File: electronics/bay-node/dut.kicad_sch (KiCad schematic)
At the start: 26 parts, among them J5 AUX, J6 CAM, Q2 2N7002, Q3 2N7002, U10 INA226AIDGSR, U9 TPS2553DBVR

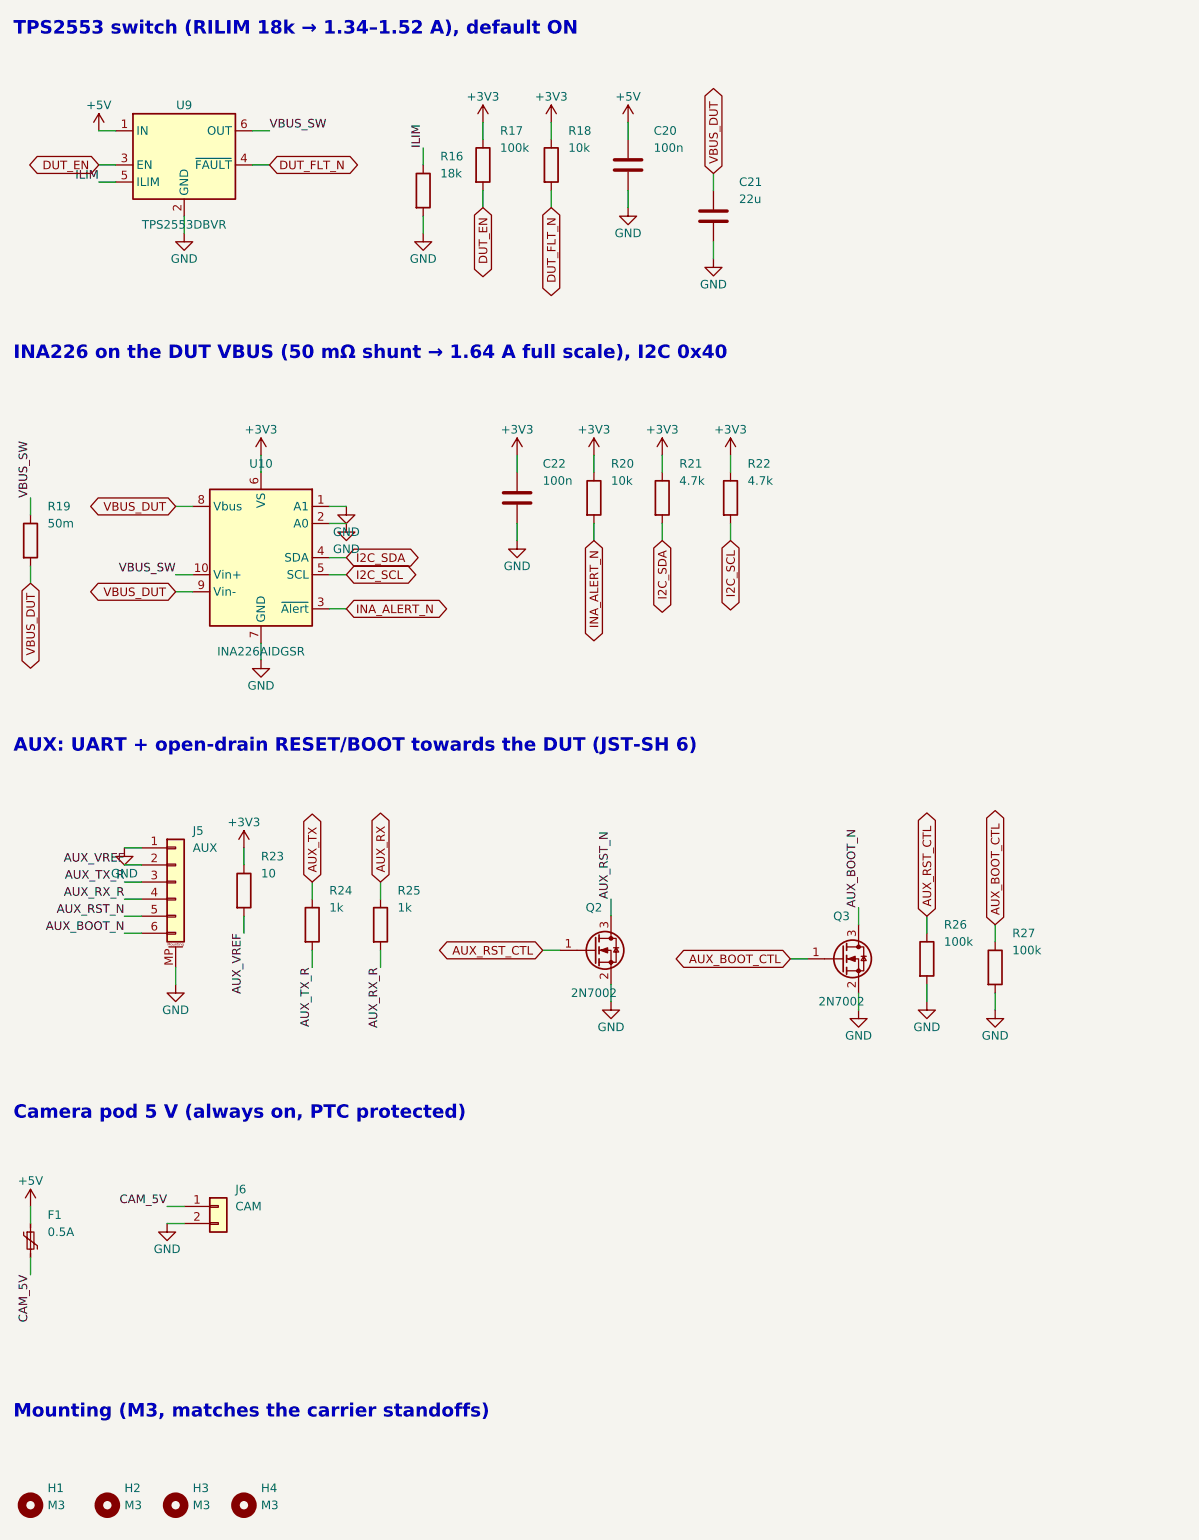
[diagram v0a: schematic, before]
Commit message: Schematics: draw real wires and an overview block diagram
The generator used to connect every pin through a net label only. Now,
in each block, the part with the most pins is the anchor and the
two-pin parts that share a signal with one of its side pins hang off
that pin on a real wire; parts chained behind them (R -> C -> GND)
stack underneath, and anchor-less blocks (pull-ups, reset/boot
buttons) are adopted by the anchor they connect to. Power symbols on
side pins point outward; power-flag references are hidden.

The root sheet becomes a block diagram: the supply rails each sheet
uses across the top, and one lane per pair of sheets listing the
signals they share.

Every wired net still carries one label, so net names, ERC (0) and the
PCB's schematic parity (0) are unchanged; the routed PCBs are untouched.

Co-Authored-By: Claude Opus 5.5 <noreply@anthropic.com>
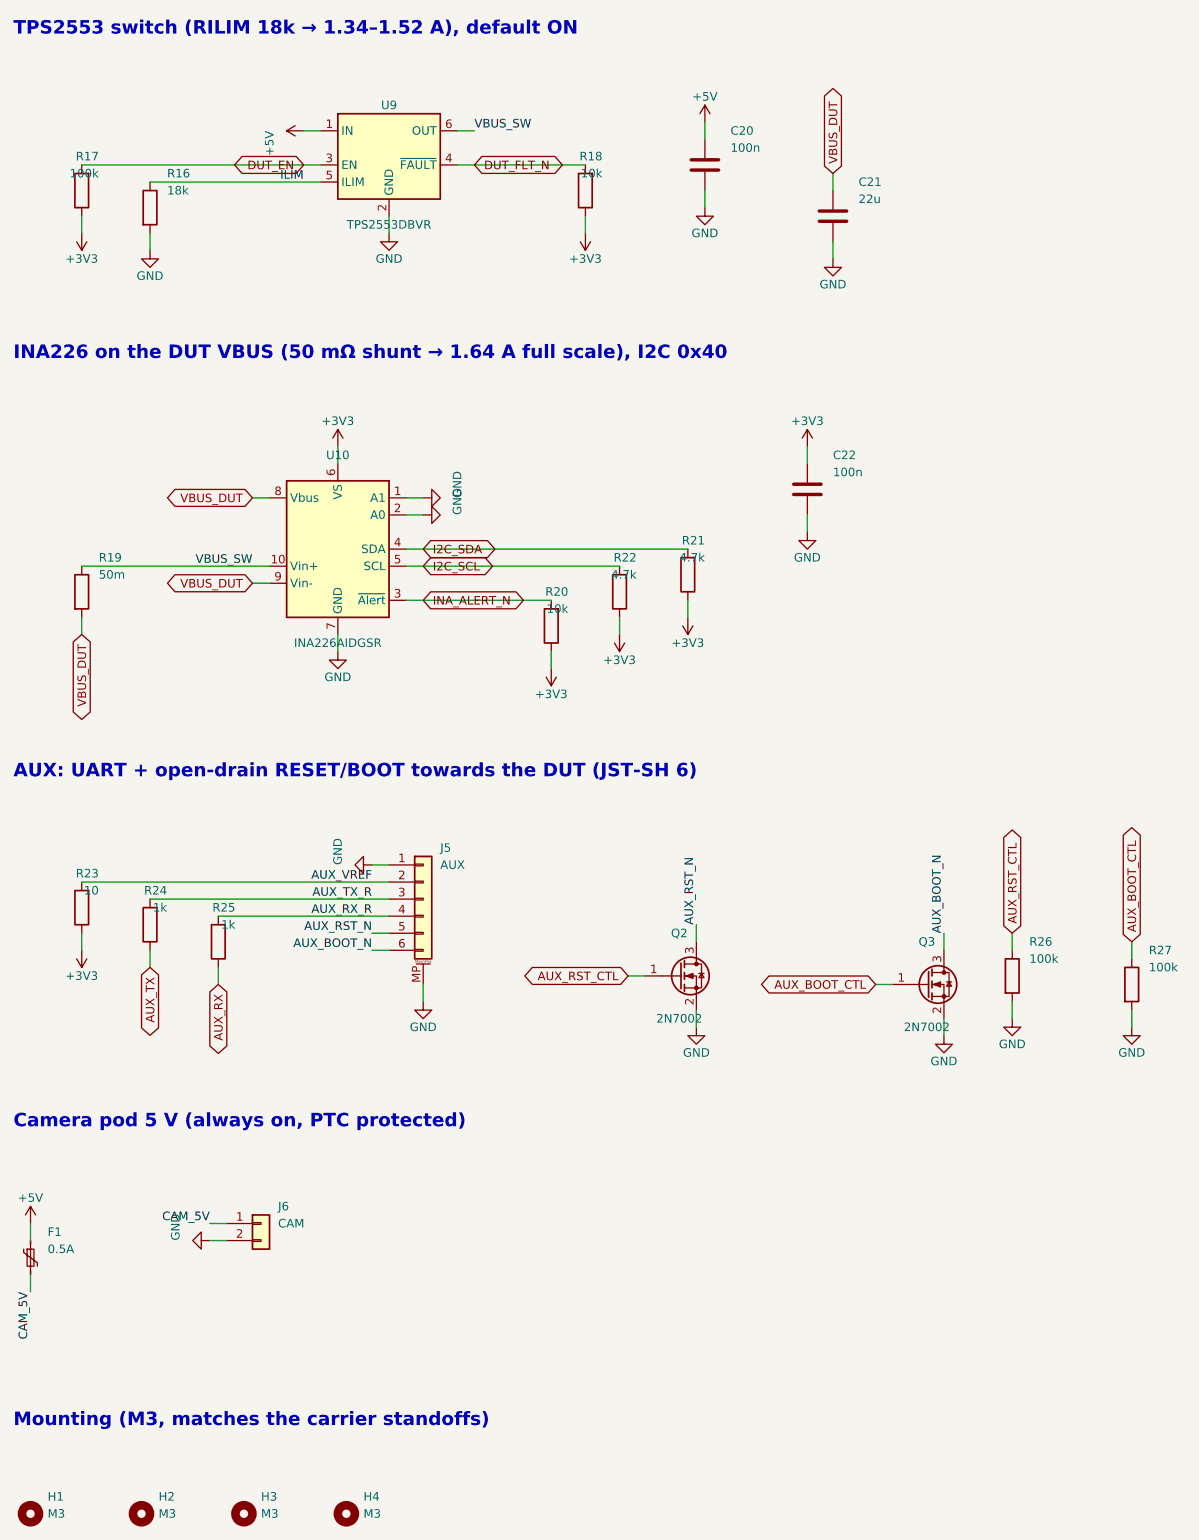
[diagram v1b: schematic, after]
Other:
- moved on the sheet: C20, C21, C22, F1, H1, H2, H3, H4, J5, J6, Q2, Q3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

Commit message: Boards v0.2: LMR51635 buck, JST PH, drawn schematics, thermal reliefs
Addresses Fabio's review of v0.1.

Bay node (rev 0.2):
- 5 V buck: LMR51635YDDCR (60 V, 3.5 A, synchronous, 1.1 MHz) with a
  3.3 uH FXL0630, 3 x 22 uF out, 2 x 10 uF + 100 nF in, FB 120k/22k
  (5.16 V), EN 1M/100k UVLO (13.5 V on, 10.8 V off). Replaces the
  TPS54360B, its Schottky and compensation network. CIN straddles the
  VIN/GND pins on solid top-side islands with vias to In1 (TI SLUSF64B).
- 24 V in/out on JST PH (carrier notches resized, rack.yaml pwr_y).
- Power nets named along the path: 24V_BUS -> +24V -> +5V -> DUT_5V_SW
  -> shunt -> DUT_5V; the INA226 visibly runs from +3V3.
- Stackup S+GND / GND / PWR / S+GND: In2 carries +5V, +3V3 under the
  ESP32 and a protected 24 V bus strip. Outer GND pours kept (without
  them Freerouting left ~25 connections unrouted).

Power hub (rev 0.2): JST VH input instead of the screw terminal, JST PH
row outputs, eFuse limit 1.6 A (RILIM 7.5k) to protect the 2 A contacts.

Generator:
- eda.py: drawn schematic mode (sch= placement, Sheet.wire/tag/frame,
  rotated/mirrored symbols, automatic junctions, per-island labels and
  checks that no wire touches another net); all seven sheets redrawn.
- pcbgen.py: thermal reliefs on every pour (+ <board>.kicad_dru for
  single spokes on fine pitch), configurable inner layers, per-zone
  deferral, fixed vias, DRC-driven fix-up for isolated GND pads.
- JLC CPL fix for the LMR51635 (270 deg); BOM, cables, viewer, docs.

ERC 0, DRC 0 copper errors, 0 unconnected, schematic parity 0 on both.

Co-Authored-By: Claude Opus 5.5 <noreply@anthropic.com>
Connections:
- net ILIM renamed DUT_ILIM
- net VBUS_DUT renamed DUT_5V
- net VBUS_SW renamed DUT_5V_SW
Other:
- note added: "AUX: UART + open-drain RESET / BOOT towards the DUT (JST SH 6)"
- note added: "Camera pod 5 V (always on, PTC protected, JST PH)"
- note added: "DUT power path: +5V → TPS2553 switch → 50 mΩ shunt → DUT_5V (DUT port VBUS), INA226 across the shunt"
- note added: "I2C pull-ups"
- note removed: "AUX: UART + open-drain RESET/BOOT towards the DUT (JST-SH 6)"
- note removed: "Camera pod 5 V (always on, PTC protected)"
- note removed: "INA226 on the DUT VBUS (50 mΩ shunt → 1.64 A full scale), I2C 0x40"
- note removed: "TPS2553 switch (RILIM 18k → 1.34–1.52 A), default ON"
- moved on the sheet: C20, C21, C22, F1, H1, H2, H3, H4, J5, J6, Q2, Q3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

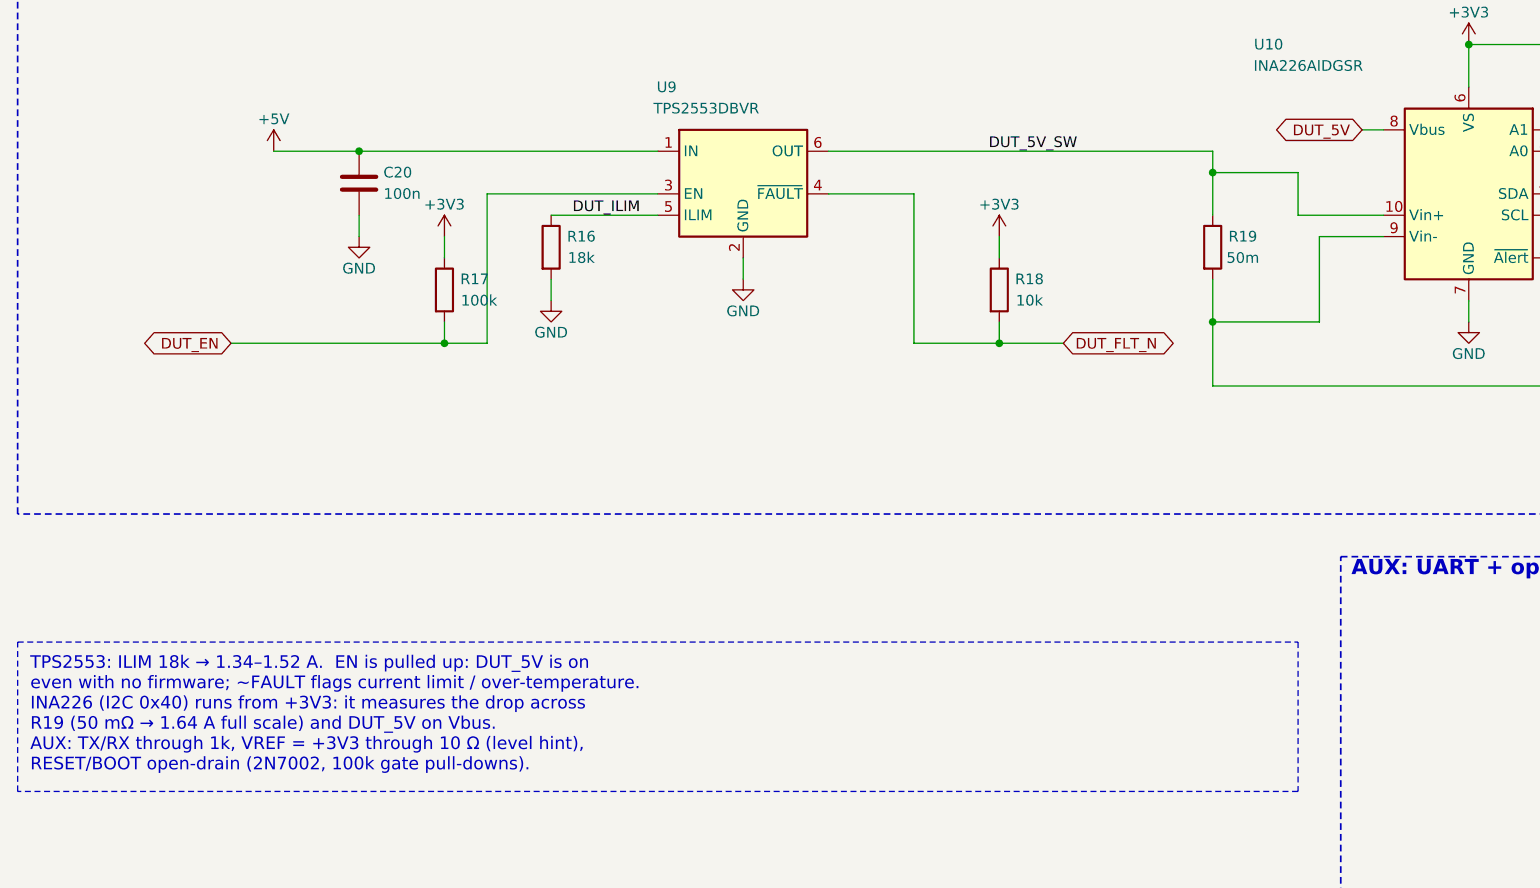
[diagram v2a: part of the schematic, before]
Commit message: Bay node: Kelvin shunt for the INA226, hand-routed USB High-Speed path
Kelvin shunt (review finding B4)
- R19 is Device:R_Shunt on bench:R_1206_3216Metric_Kelvin: the stock 1206
  pads plus a tented sense pad on the inner edge of each terminal, tied by
  net-tie pad groups (generated by the new electronics/tools/footprints.py).
- The INA226 reads SHUNT_P/SHUNT_N from those pads only, instead of tapping
  DUT_5V ~2.8 mm down the load track (~4-5 % gain error).

USB High-Speed in classic mode (finding B3)
- usb_hs_routes() in design.py draws the J3 -> U4 -> U5 -> U6 -> U8 -> J4
  chain as coupled pairs on F.Cu over In1 (0.25/0.15 mm, ~90 ohm estimate),
  ESD parts in flow-through, one B.Cu crossover between the FSUSB42s with
  three length bumps on PCPATH_DP; skew 1.8 mm J3 -> J4.  U4, U5, U6, U8,
  C17, C18, R24, R25 moved or rotated for a straight path.
- pcbgen.py: b.pcb["tracks"] draws locked tracks before routing (Freerouting
  keeps protected wiring and routes around it); fixed vias are locked too;
  pass-through vias left by Freerouting are dropped after the session import.

ERC 0/0, DRC 0 errors / 0 warnings, 0 unconnected, parity 0, JLC DFM audit
0 findings.  The power hub still regenerates clean with the new generator
(its committed outputs are unchanged).

Co-Authored-By: Claude Opus 5.5 <noreply@anthropic.com>
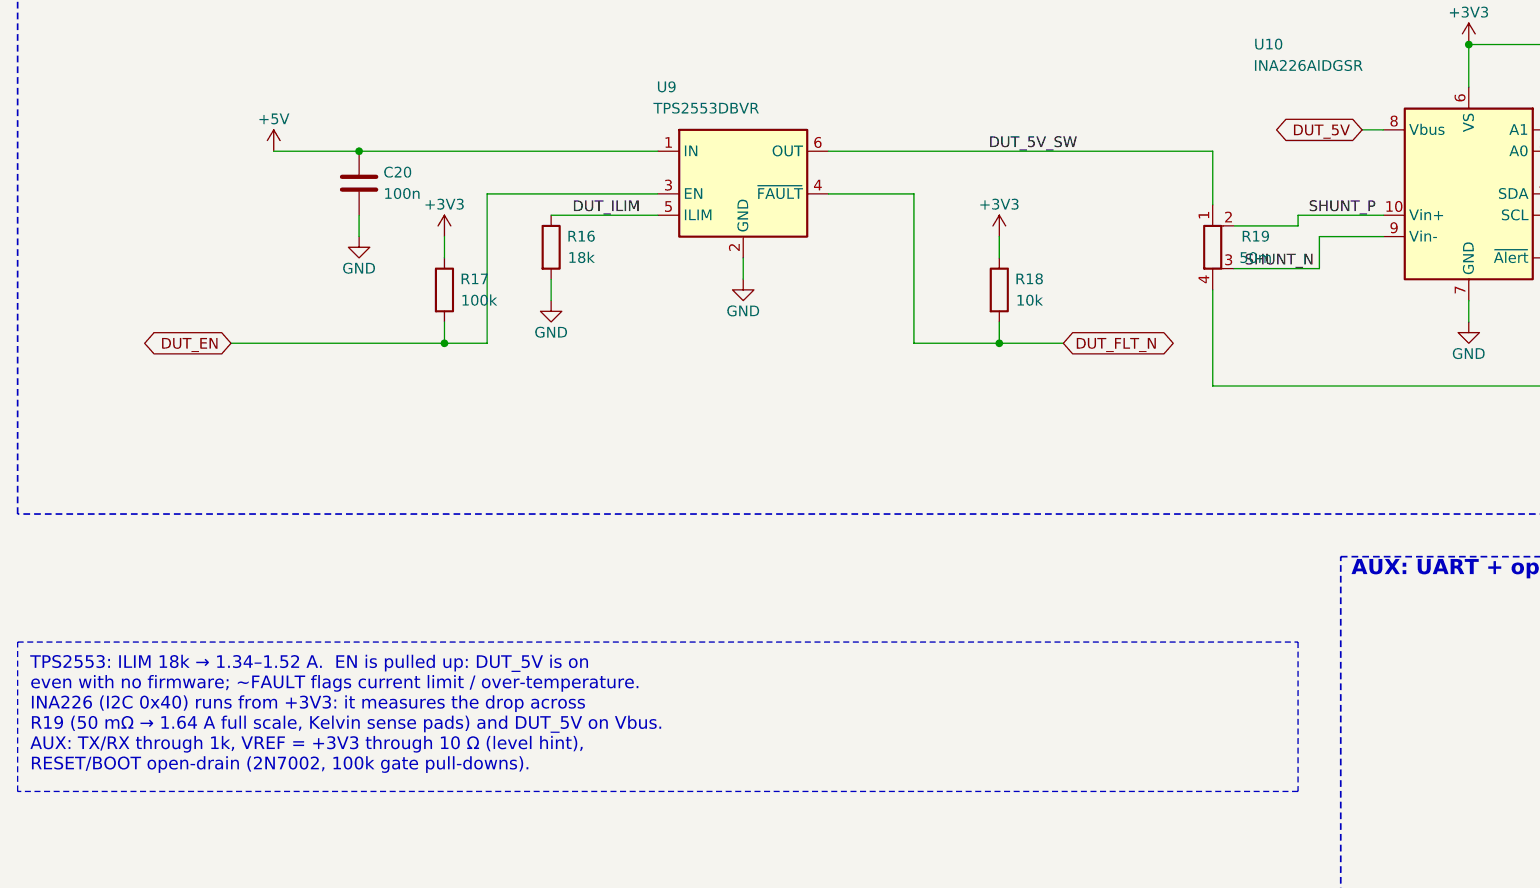
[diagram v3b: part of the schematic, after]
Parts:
- R19: footprint Resistor_SMD:R_1206_3216Metric -> bench:R_1206_3216Metric_Kelvin; symbol Device:R -> Device:R_Shunt
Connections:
- net DUT_5V: now also R19.4; no longer R19.2, U10.9 (Vin-)
- net DUT_5V_SW: no longer U10.10 (Vin+)
- new net SHUNT_N: R19.3, U10.9 (Vin-)
- new net SHUNT_P: R19.2, U10.10 (Vin+)
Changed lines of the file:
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@@
 	)
 	(symbol
-		(lib_id "Device:R")
+		(lib_id "Device:R_Shunt")
 		(at 157.48 85.09 0)
 		(unit 1)
@@
 		(fields_autoplaced yes)
 		(property "Reference" "R19"
-			(at 161.071 83.82 0)
+			(at 162.595 83.82 0)
 			(effects
 				(font
@@
 		)
 		(property "Value" "50m"
-			(at 161.071 86.36 0)
+			(at 162.595 86.36 0)
 			(effects
 				(font
@@
 			)
 		)
-		(property "Footprint" "Resistor_SMD:R_1206_3216Metric"
+		(property "Footprint" "bench:R_1206_3216Metric_Kelvin"
 			(at 157.48 85.09 0)
 			(effects
@@
 		(pin "2"
 		)
+		(pin "3"
+		)
+		(pin "4"
+		)
 		(instances
 			(project "bay-node"
@@
 		(pts
 			(xy 157.48 73.66)
-			(xy 157.48 81.28)
+			(xy 157.48 80.01)
 		)
 		(stroke
@@
 	(wire
 		(pts
-			(xy 157.48 88.9)
+			(xy 157.48 90.17)
 			(xy 157.48 101.6)
 		)
@@
 	(wire
 		(pts
-			(xy 157.48 76.2)
-			(xy 167.64 76.2)
+			(xy 160.02 82.55)
+			(xy 167.64 82.55)
 		)
 		(stroke
@@
 	(wire
 		(pts
-			(xy 167.64 76.2)
+			(xy 167.64 82.55)
 			(xy 167.64 81.28)
 		)
@@
 	(wire
 		(pts
-			(xy 157.48 93.98)
-			(xy 170.18 93.98)
+			(xy 160.02 87.63)
+			(xy 170.18 87.63)
 		)
 		(stroke
@@
 	(wire
 		(pts
-			(xy 170.18 93.98)
+			(xy 170.18 87.63)
 			(xy 170.18 83.82)
 		)
@@
 	)
 	(junction
-		(at 157.48 76.2)
-		(diameter 0)
-		(color 0 0 0 0)
-	)
-	(junction
-		(at 157.48 93.98)
-		(diameter 0)
-		(color 0 0 0 0)
-	)
-	(junction
 		(at 187.96 60.96)
 		(diameter 0)
@@
 		)
 	)
+	(label "SHUNT_P"
+		(at 168.91 81.28 0)
+		(fields_autoplaced yes)
+		(effects
+			(font
+				(size 1.27 1.27)
+			)
+			(justify left bottom)
+		)
+	)
+	(label "SHUNT_N"
+		(at 161.29 87.63 0)
+		(fields_autoplaced yes)
+		(effects
+			(font
+				(size 1.27 1.27)
+			)
+			(justify left bottom)
+		)
+	)
 	(label "CAM_5V"
 		(at 331.47 137.16 0)
@@
 		)
 	)
-	(text_box "TPS2553: ILIM 18k → 1.34–1.52 A.  EN is pulled up: DUT_5V is on\n  even with no firmware; ~FAULT flags current limit / over-temperature.\nINA226 (I2C 0x40) runs from +3V3: it measures the drop across\n  R19 (50 mΩ → 1.64 A full scale) and DUT_5V on Vbus.\nAUX: TX/RX through 1k, VREF = +3V3 through 10 Ω (level hint),\n  RESET/BOOT open-drain (2N7002, 100k gate pull-downs)."
+	(text_box "TPS2553: ILIM 18k → 1.34–1.52 A.  EN is pulled up: DUT_5V is on\n  even with no firmware; ~FAULT flags current limit / over-temperature.\nINA226 (I2C 0x40) runs from +3V3: it measures the drop across\n  R19 (50 mΩ → 1.64 A full scale, Kelvin sense pads) and DUT_5V on Vbus.\nAUX: TX/RX through 1k, VREF = +3V3 through 10 Ω (level hint),\n  RESET/BOOT open-drain (2N7002, 100k gate pull-downs)."
 		(exclude_from_sim no)
 		(at 15.24 132.08 0)
